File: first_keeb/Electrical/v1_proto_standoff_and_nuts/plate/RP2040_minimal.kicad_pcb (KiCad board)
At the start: 2 copper layers, 80 x 80 mm, 8 parts

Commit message: stm it up
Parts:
- H1, H2, H3: value M3_Threaded_Insert -> MountingHole_3.2mm_M3; footprint MountingHole:M3_Threaded_Insert -> MountingHole:MountingHole_3.2mm_M3
- moved H1 6.00 mm to (79.0, 86.0)
- moved H2 6.00 mm to (121.0, 86.0)
- moved H3 6.00 mm to (100.0, 123.0)
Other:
- board size 80 x 80 mm -> 66 x 66 mm
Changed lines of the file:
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@@
     (pad "" np_thru_hole circle (at 0 0) (size 2.3 2.3) (drill 2.3) (layers "F&B.Cu" "*.Mask"))
   )
-  (footprint "MountingHole:M3_Threaded_Insert" (layer "B.Cu")
-    (at 100 129 180)
+  (footprint "MountingHole:MountingHole_3.2mm_M3" (layer "B.Cu")
+    (at 100 123 180)
+    (descr "Mounting Hole 3.2mm, no annular, M3")
+    (tags "mounting hole 3.2mm no annular m3")
     (property "Sheetfile" "RP2040_minimal.kicad_sch")
     (property "Sheetname" "")
     (property "ki_description" "Mounting Hole with connection")
     (property "ki_keywords" "mounting hole")
-    (attr smd)
-    (fp_text reference "H3" (at 0 0.5 unlocked) (layer "B.SilkS")
-        (effects (font (size 1 1) (thickness 0.15)) (justify mirror))
-    )
-    (fp_text value "M3_Threaded_Insert" (at 0 -1 unlocked) (layer "B.Fab")
-        (effects (font (size 1 1) (thickness 0.15)) (justify mirror))
-    )
-    (fp_text user "${REFERENCE}" (at 0 -2.5 unlocked) (layer "B.Fab")
+    (attr exclude_from_pos_files exclude_from_bom)
+    (fp_text reference "H3" (at 0 4.2) (layer "B.SilkS")
+        (effects (font (size 1 1) (thickness 0.15)) (justify mirror))
+    )
+    (fp_text value "MountingHole_3.2mm_M3" (at 0 -4.2) (layer "B.Fab")
+        (effects (font (size 1 1) (thickness 0.15)) (justify mirror))
+    )
+    (fp_text user "${REFERENCE}" (at 0 0) (layer "B.Fab")
         (effects (font (size 1 1) (thickness 0.15)) (justify mirror))
     )
     (fp_circle (center 0 0) (end 3.2 0)
-      (stroke (width 0.12) (type default)) (fill none) (layer "Cmts.User"))
-    (pad "" np_thru_hole circle (at 0 0 180) (size 4.2 4.2) (drill 4.2) (layers "F&B.Cu" "*.Mask"))
-    (pad "1" smd circle (at 0 0 180) (size 6.2 6.2) (layers "B.Cu" "B.Mask"))
+      (stroke (width 0.15) (type solid)) (fill none) (layer "Cmts.User"))
+    (fp_circle (center 0 0) (end 3.45 0)
+      (stroke (width 0.05) (type solid)) (fill none) (layer "B.CrtYd"))
+    (pad "" np_thru_hole circle (at 0 0 180) (size 3.2 3.2) (drill 3.2) (layers "*.Cu" "*.Mask"))
   )
-  (footprint "MountingHole:M3_Threaded_Insert" (layer "B.Cu")
-    (at 127 86 180)
+  (footprint "MountingHole:MountingHole_3.2mm_M3" (layer "B.Cu")
+    (at 121 86 180)
+    (descr "Mounting Hole 3.2mm, no annular, M3")
+    (tags "mounting hole 3.2mm no annular m3")
     (property "Sheetfile" "RP2040_minimal.kicad_sch")
     (property "Sheetname" "")
     (property "ki_description" "Mounting Hole with connection")
     (property "ki_keywords" "mounting hole")
-    (attr smd)
-    (fp_text reference "H2" (at 0 0.5 unlocked) (layer "B.SilkS")
-        (effects (font (size 1 1) (thickness 0.15)) (justify mirror))
-    )
-    (fp_text value "M3_Threaded_Insert" (at 0 -1 unlocked) (layer "B.Fab")
-        (effects (font (size 1 1) (thickness 0.15)) (justify mirror))
-    )
-    (fp_text user "${REFERENCE}" (at 0 -2.5 unlocked) (layer "B.Fab")
+    (attr exclude_from_pos_files exclude_from_bom)
+    (fp_text reference "H2" (at 0 4.2) (layer "B.SilkS")
+        (effects (font (size 1 1) (thickness 0.15)) (justify mirror))
+    )
+    (fp_text value "MountingHole_3.2mm_M3" (at 0 -4.2) (layer "B.Fab")
+        (effects (font (size 1 1) (thickness 0.15)) (justify mirror))
+    )
+    (fp_text user "${REFERENCE}" (at 0 0) (layer "B.Fab")
         (effects (font (size 1 1) (thickness 0.15)) (justify mirror))
     )
     (fp_circle (center 0 0) (end 3.2 0)
-      (stroke (width 0.12) (type default)) (fill none) (layer "Cmts.User"))
-    (pad "" np_thru_hole circle (at 0 0 180) (size 4.2 4.2) (drill 4.2) (layers "F&B.Cu" "*.Mask"))
-    (pad "1" smd circle (at 0 0 180) (size 6.2 6.2) (layers "B.Cu" "B.Mask"))
+      (stroke (width 0.15) (type solid)) (fill none) (layer "Cmts.User"))
+    (fp_circle (center 0 0) (end 3.45 0)
+      (stroke (width 0.05) (type solid)) (fill none) (layer "B.CrtYd"))
+    (pad "" np_thru_hole circle (at 0 0 180) (size 3.2 3.2) (drill 3.2) (layers "*.Cu" "*.Mask"))
   )
-  (footprint "MountingHole:M3_Threaded_Insert" (layer "B.Cu")
-    (at 73 86 180)
+  (footprint "MountingHole:MountingHole_3.2mm_M3" (layer "B.Cu")
+    (at 79 86 180)
+    (descr "Mounting Hole 3.2mm, no annular, M3")
+    (tags "mounting hole 3.2mm no annular m3")
     (property "Sheetfile" "RP2040_minimal.kicad_sch")
     (property "Sheetname" "")
     (property "ki_description" "Mounting Hole with connection")
     (property "ki_keywords" "mounting hole")
-    (attr smd)
-    (fp_text reference "H1" (at 0 0.5 unlocked) (layer "B.SilkS")
-        (effects (font (size 1 1) (thickness 0.15)) (justify mirror))
-    )
-    (fp_text value "M3_Threaded_Insert" (at 0 -1 unlocked) (layer "B.Fab")
-        (effects (font (size 1 1) (thickness 0.15)) (justify mirror))
-    )
-    (fp_text user "${REFERENCE}" (at 0 -2.5 unlocked) (layer "B.Fab")
+    (attr exclude_from_pos_files exclude_from_bom)
+    (fp_text reference "H1" (at 0 4.2) (layer "B.SilkS")
+        (effects (font (size 1 1) (thickness 0.15)) (justify mirror))
+    )
+    (fp_text value "MountingHole_3.2mm_M3" (at 0 -4.2) (layer "B.Fab")
+        (effects (font (size 1 1) (thickness 0.15)) (justify mirror))
+    )
+    (fp_text user "${REFERENCE}" (at 0 0) (layer "B.Fab")
         (effects (font (size 1 1) (thickness 0.15)) (justify mirror))
     )
     (fp_circle (center 0 0) (end 3.2 0)
-      (stroke (width 0.12) (type default)) (fill none) (layer "Cmts.User"))
-    (pad "" np_thru_hole circle (at 0 0 180) (size 4.2 4.2) (drill 4.2) (layers "F&B.Cu" "*.Mask"))
-    (pad "1" smd circle (at 0 0 180) (size 6.2 6.2) (layers "B.Cu" "B.Mask"))
+      (stroke (width 0.15) (type solid)) (fill none) (layer "Cmts.User"))
+    (fp_circle (center 0 0) (end 3.45 0)
+      (stroke (width 0.05) (type solid)) (fill none) (layer "B.CrtYd"))
+    (pad "" np_thru_hole circle (at 0 0 180) (size 3.2 3.2) (drill 3.2) (layers "*.Cu" "*.Mask"))
   )
   (gr_poly
@@
     )
     (stroke (width 0.021144) (type solid)) (fill solid) (layer "F.Mask"))
-  (gr_circle (center 100 100) (end 140 100)
+  (gr_circle (center 100 100) (end 133 100)
     (stroke (width 0.2) (type default)) (fill none) (layer "Edge.Cuts"))
   (zone (net 0) (net_name "") (layers "F&B.Cu") (hatch edge 0.5)

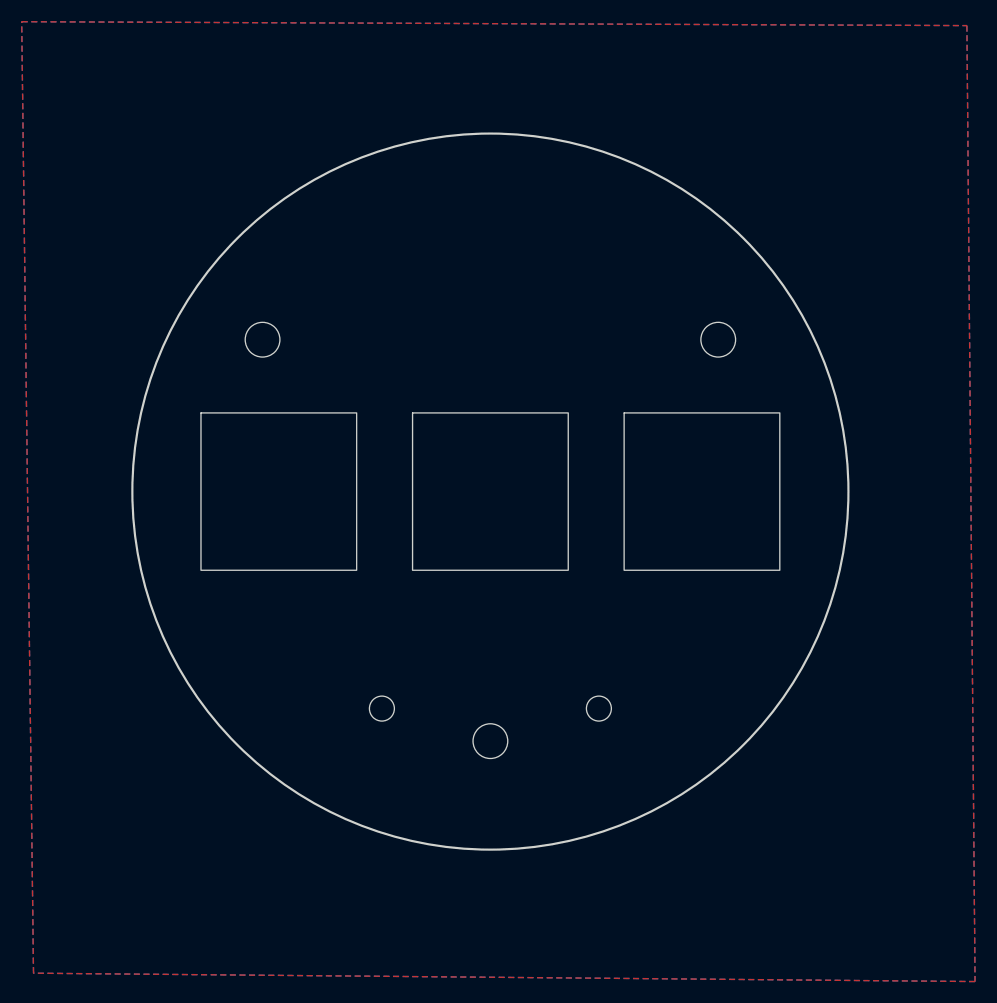
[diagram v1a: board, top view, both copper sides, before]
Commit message: creates plate for pcb
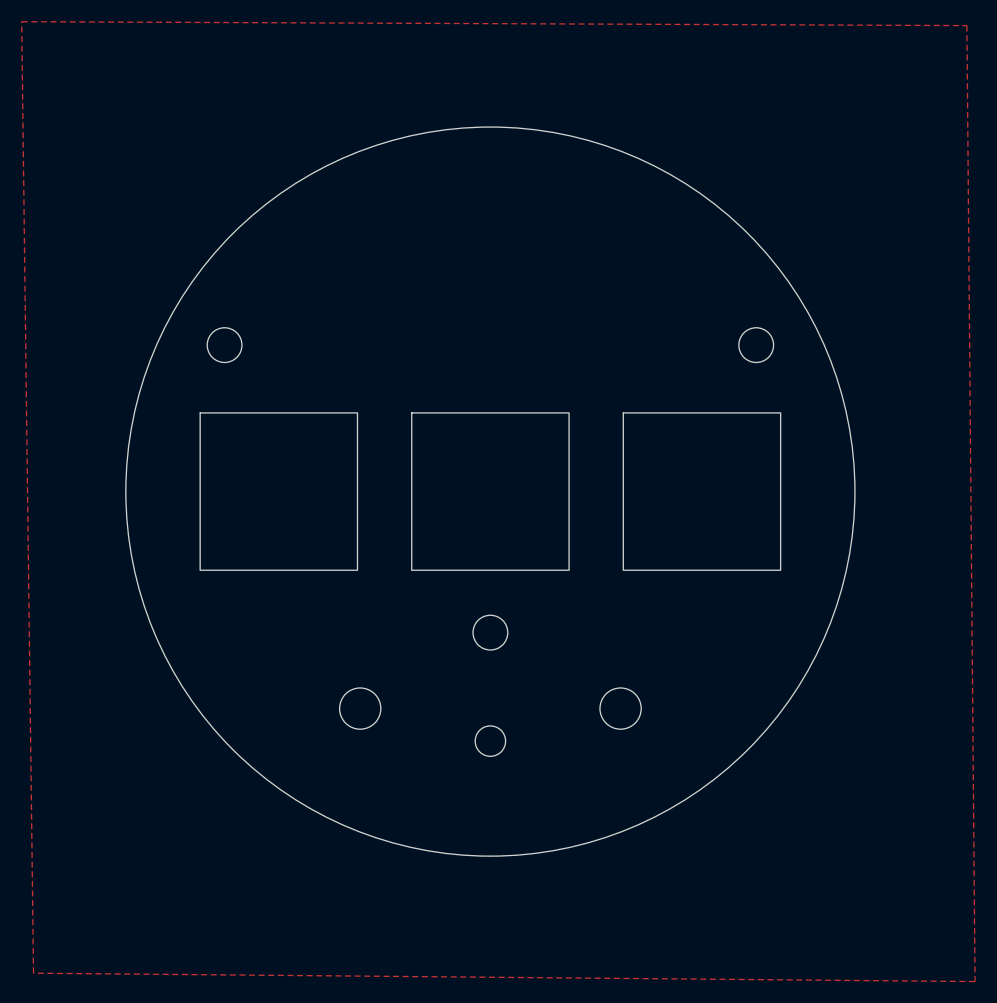
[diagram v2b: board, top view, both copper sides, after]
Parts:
- removed the REF** at (90.0, 120.0)
- removed the REF** at (110.0, 120.0)
- added REF**: MountingHole_3.7mm, MountingHole:MountingHole_3.7mm, F.Cu at (88.0, 120.0)
- added REF**: MountingHole_3.7mm, MountingHole:MountingHole_3.7mm, F.Cu at (112.0, 120.0)
- added REF**: MountingHole_2.7mm, MountingHole:MountingHole_2.7mm, F.Cu at (100.0, 123.0)
- moved H3 10.0 mm to (100.0, 113.0)
- moved H1 3.54 mm to (75.5, 86.5)
- moved H2 3.54 mm to (124.5, 86.5)
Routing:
- removed copper zone on B.Cu, net GND
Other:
- board size 66 x 66 mm -> 67.2 x 67.2 mm

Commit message: changes to ws2812b 5050 and moves 5v power rail to mostly 4th layer
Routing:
- added copper zone on B.Cu, net GND

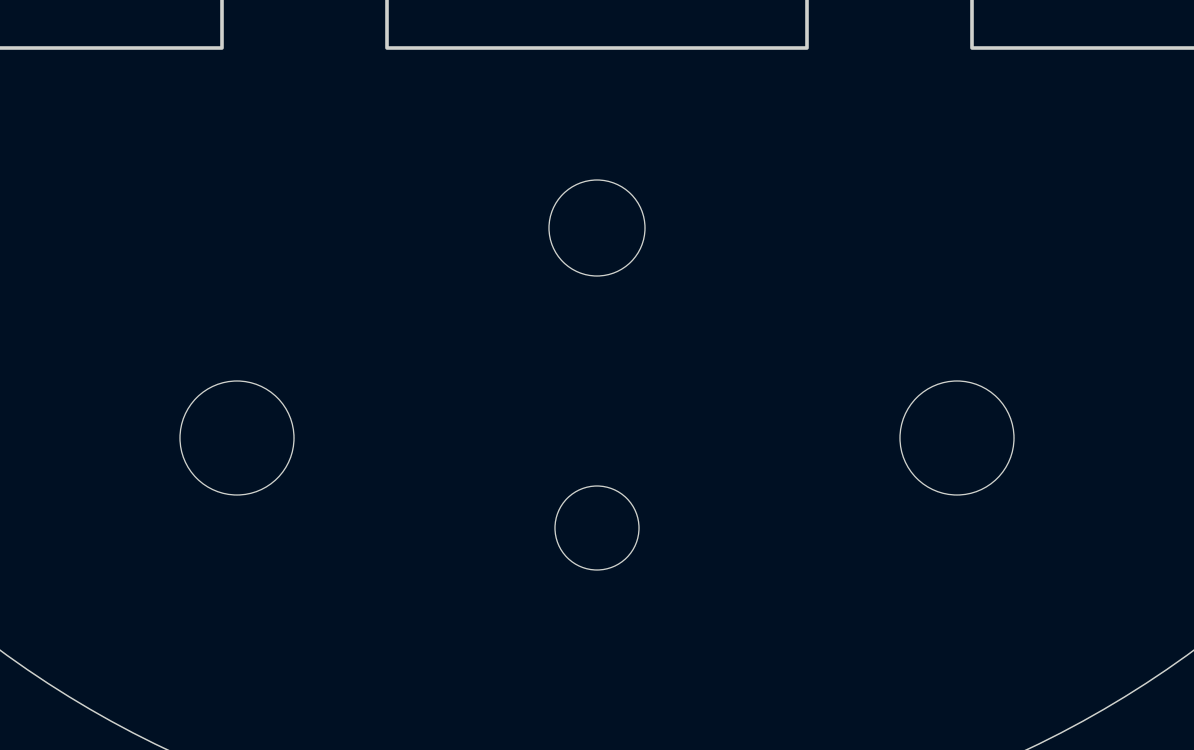
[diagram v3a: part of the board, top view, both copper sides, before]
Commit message: v1 stm ordered
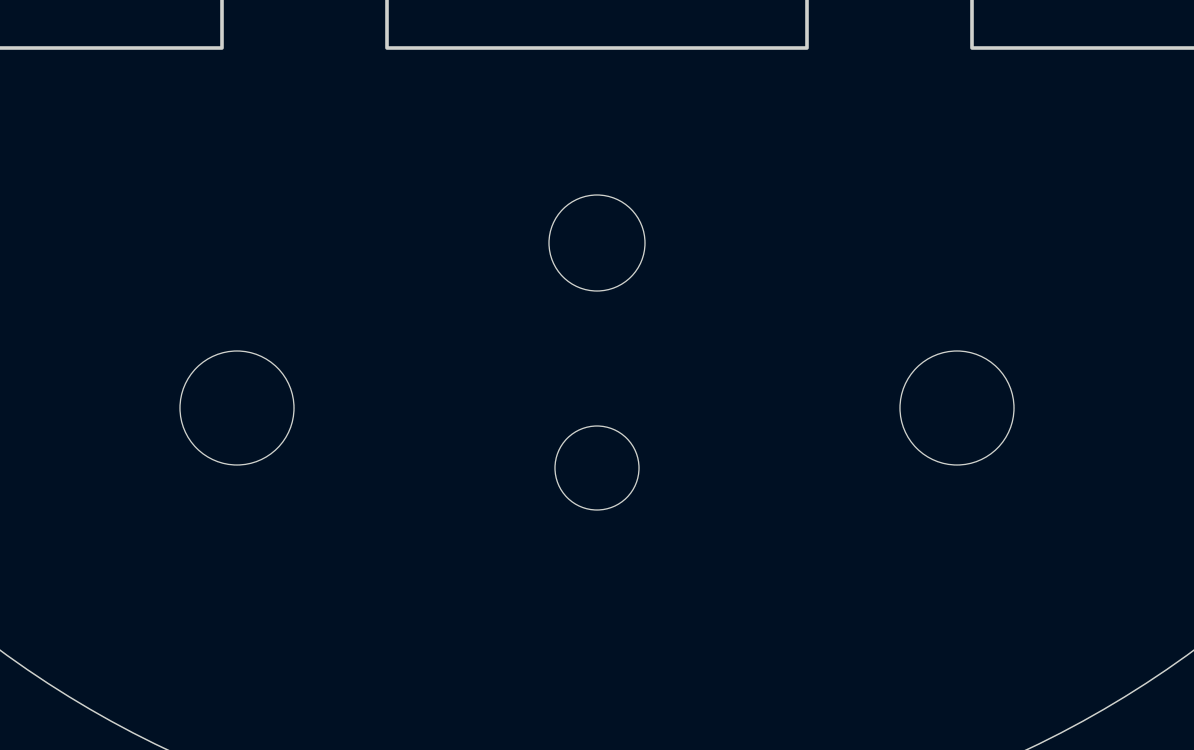
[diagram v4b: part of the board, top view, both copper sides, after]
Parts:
- moved REF** 2.00 mm to (100.0, 121.0)
- moved REF** 1.00 mm to (88.0, 119.0)
- moved REF** 1.00 mm to (112.0, 119.0)
- moved H3 0.50 mm to (100.0, 113.5)

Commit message: no more line in 3d print
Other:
- board text added: "H2"

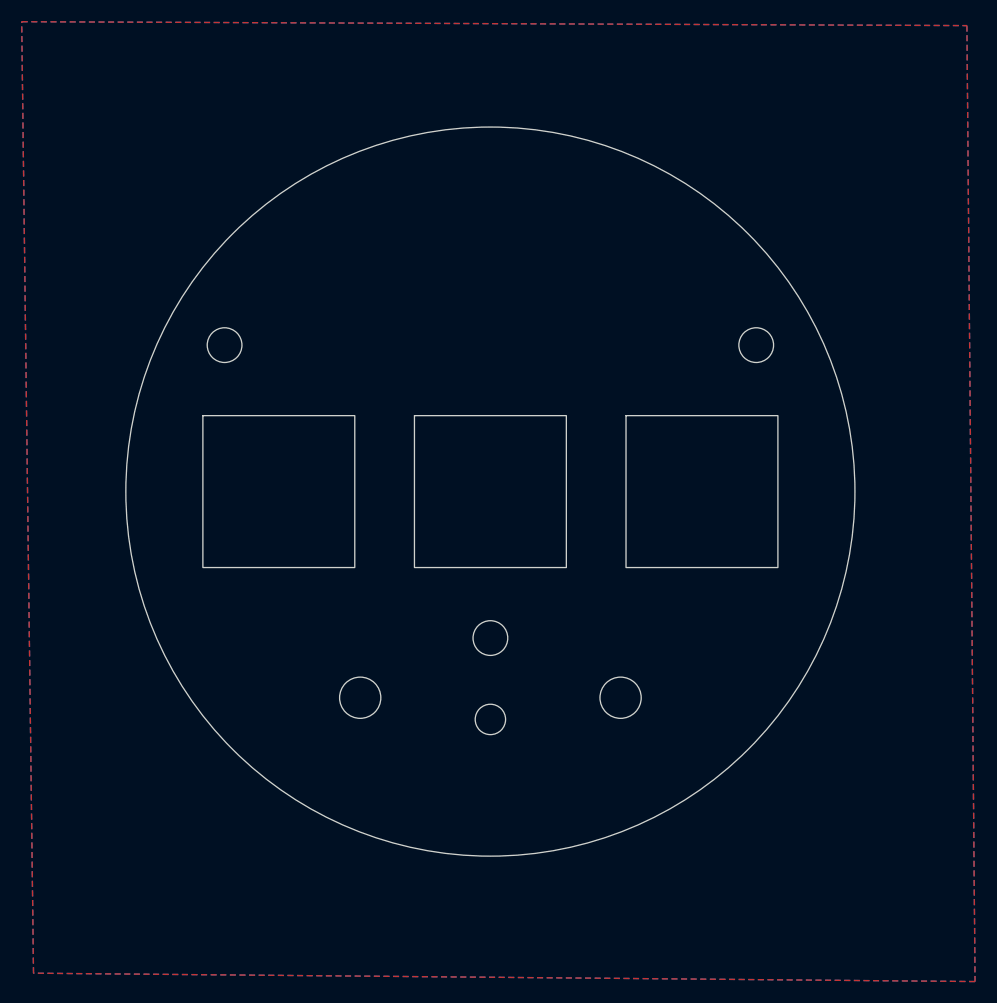
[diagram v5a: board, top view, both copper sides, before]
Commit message: moves pcb components down to make more space, and fixes case
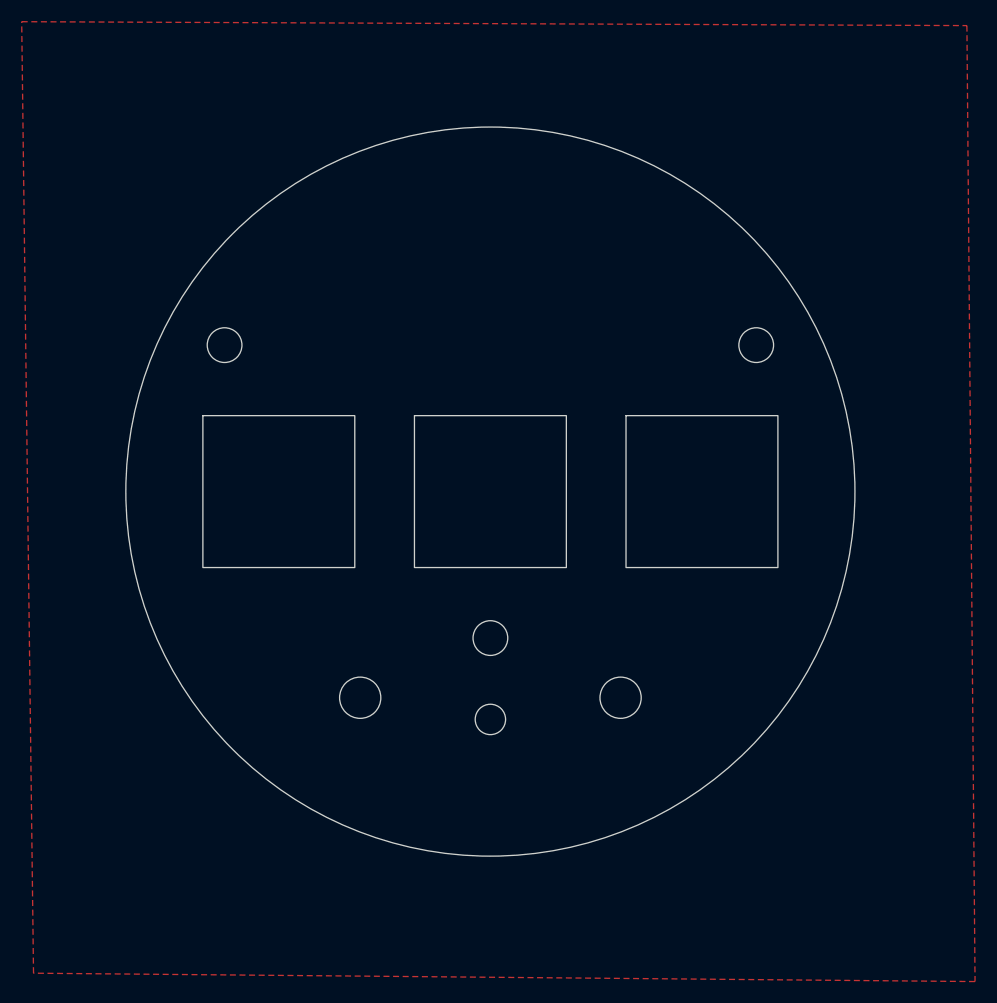
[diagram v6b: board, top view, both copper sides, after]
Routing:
- removed copper zone on B.Cu, net GND
